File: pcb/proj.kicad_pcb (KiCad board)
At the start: 2 copper layers, 125 x 185 mm, 125 parts, among them J1 Conn_02x05_Odd_Even, SW1 Reset, SW10 8, SW11 9, SW12 /, SW13 Deg/Rad, SW14 Clear, SW15 4, SW16 5, SW17 6, SW18 X, SW19 Constants, SW2 Y/Stats, SW20 Del, SW21 1, SW22 2, SW23 3, SW24 -, SW25 Alpha, SW26 (/), SW27 Sin(x)/Sin-1(x), SW28 Cos(x)/Cos-1(x), SW29 Tan(x)/Tan-1(x), SW3 ./,, SW30 +, SW31 2nd, SW32 Γ(x), SW33 x^y/y√x, SW34 x^2/√x, SW35 log(x)/ln(x), SW36 e^x/10^x, SW37 Graph, SW38 Programs, SW39 Left, SW4 0, SW40 Up, SW41 Right, SW42 Down, SW43 Power, SW44 FPU BOOT0, SW45 Reset, SW5 +/-, SW6 Solve/=, SW7 Sci/Norm, SW8 X/Matrix, SW9 7, U1 PIC16C74, U2 STM32F401RCTx, U3 74HC238, U4 ISL9111EH50Z-T7A, U5 SN74LVC1G32DBVR, Y1 20MHz

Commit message: v 1.2
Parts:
- removed B2: 2032, Parts:BAT_BAT-HLD-001-THM
- B1: value 2032 -> 2x AA; footprint Parts:BAT_BAT-HLD-001-THM -> Battery:BatteryHolder_MPD_BC2AAPC_2xAA
- C1, C2: footprint Capacitor_SMD:C_0402_1005Metric_Pad0.74x0.62mm_HandSolder -> Capacitor_SMD:C_1206_3216Metric_Pad1.33x1.80mm_HandSolder
- D1, D10, D11, D12, D13, D14, D15, D16, D17, D18, D19, D2, D20, D21, D22, D23, D24, D25, D26, D27, D28, D29, D3, D30, D31, D32, D33, D34, D35, D36, D37, D38, D39, D4, D40, D41, D42, D5, D6, D7, D8, D9: value BAS7002 -> S040S2R0; footprint Diode_SMD:D_SOD-523 -> Diode_SMD:D_1206_3216Metric_Pad1.42x1.75mm_HandSolder
- moved B1 11.0 mm to (142.0, 122.0), turned to -90 degrees
- moved J1 4.75 mm to (131.8, 186.8)
- moved D39 0.79 mm to (83.2, 106.2)
- moved D40 0.79 mm to (93.2, 97.8)
- moved D42 0.79 mm to (93.2, 114.8)
- moved D1 0.75 mm to (48.2, 189.0)
- moved D10 0.75 mm to (84.0, 176.8)
- moved D11 0.75 mm to (95.8, 176.8)
- moved D12 0.75 mm to (107.2, 176.8)
- moved D13 0.75 mm to (48.2, 164.5)
- moved D14 0.75 mm to (60.2, 164.5)
- moved D15 0.75 mm to (72.2, 164.5)
- moved D16 0.75 mm to (84.0, 164.5)
- moved D17 0.75 mm to (95.8, 164.5)
- moved D18 0.75 mm to (107.2, 164.5)
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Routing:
- net Net-(B1-+): track 192.7 -> 106.4 mm
- net Net-(D15-K): track 384.4 -> 370.3 mm
- net Net-(D10-K): track 380.2 -> 366.4 mm
- net Net-(D11-K): track 366.7 -> 359.1 mm
- net Net-(D14-K): track 400.8 -> 393.7 mm
- net Net-(D1-K): track 413.9 -> 407.1 mm
- net Net-(D12-K): track 343.6 -> 338.1 mm
- net Net-(D38-A): track 10.2 -> 15.5 mm
- net Net-(D42-A): track 10.2 -> 15.3 mm
- net Net-(D40-A): track 10.2 -> 15.3 mm
- net Net-(D41-A): track 10.0 -> 14.9 mm
- net FPURST: track 111.6 -> 116.4 mm
- net SWO: track 134.1 -> 138.8 mm
- net SWDIO: track 128.2 -> 132.9 mm
- net SWCLK: track 127.1 -> 131.5 mm
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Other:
- board text added: "PICalculator v1.2 Designed by: Kyle Schmerge Max Pastushkov https://github.com/kpzip/PICalculator"
- board text removed: "PICalculator v1.1 Designed by: Kyle Schmerge Max Pastushkov Janet Shen https://github.com/kpzip/PICalculator"

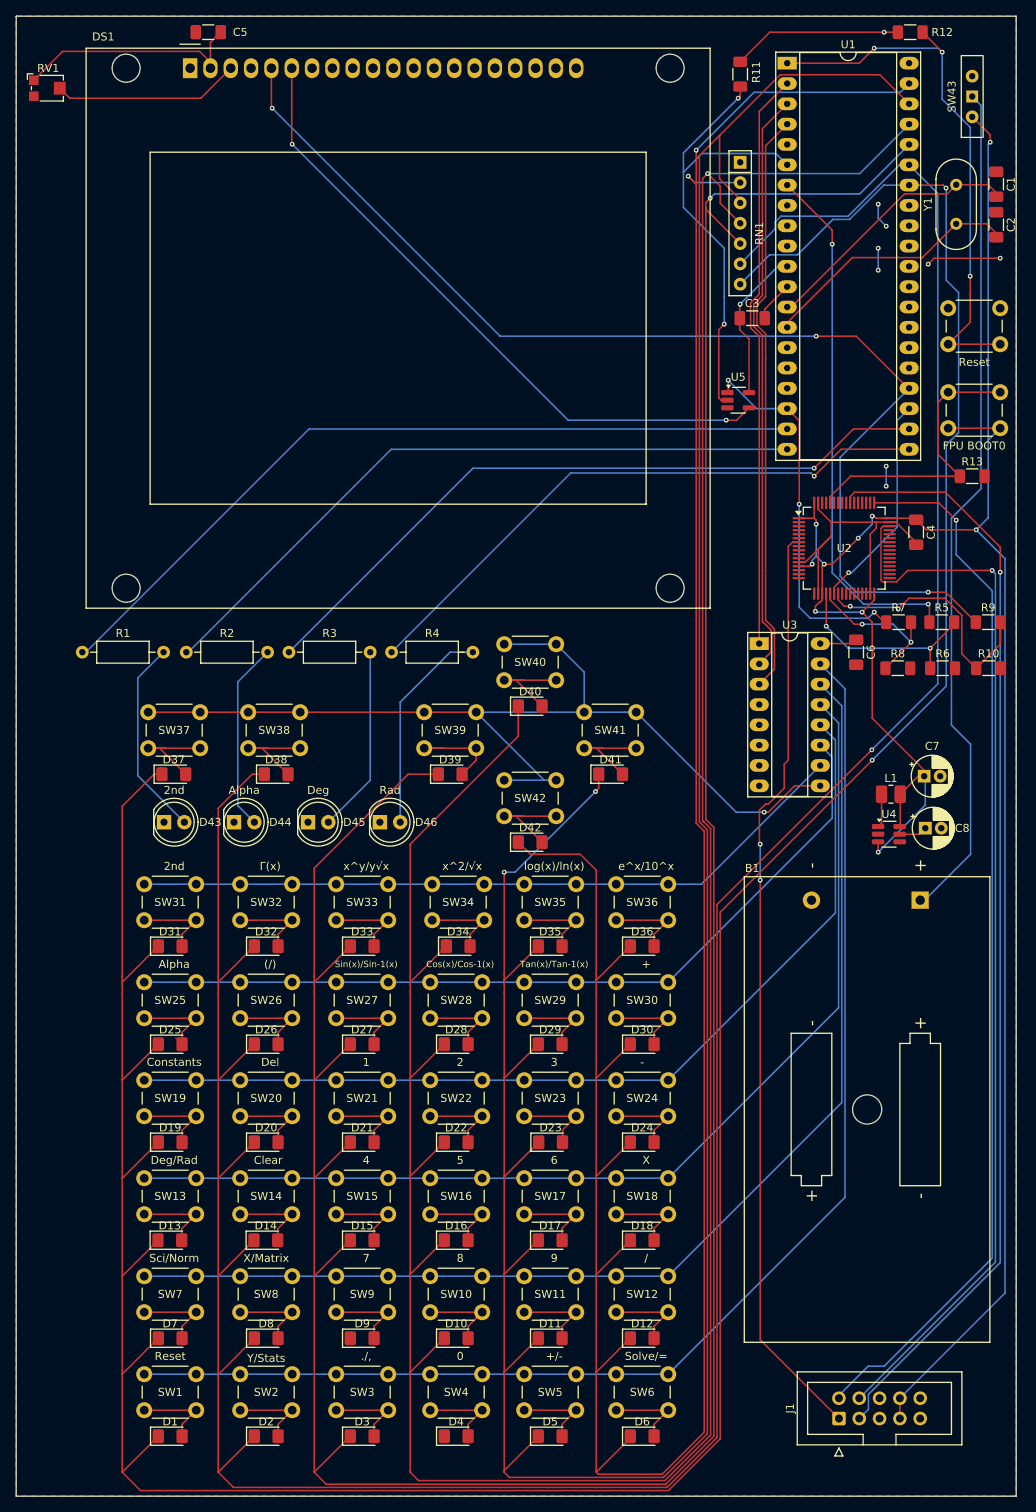
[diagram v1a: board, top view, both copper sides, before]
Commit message: update schematics + add CO RDY trace
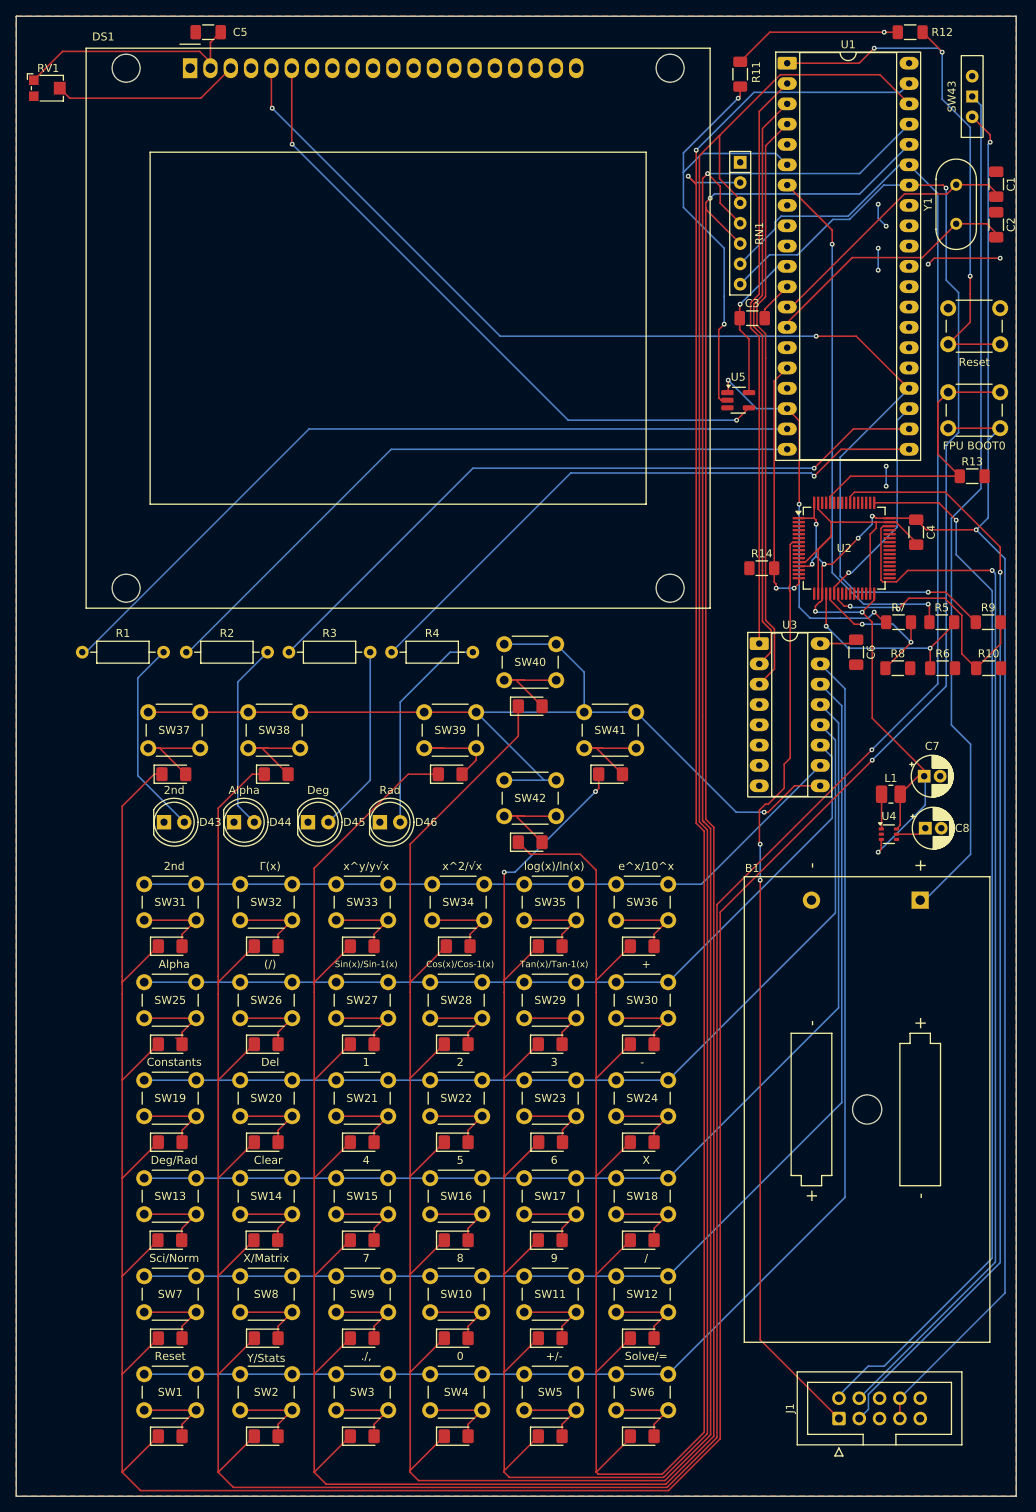
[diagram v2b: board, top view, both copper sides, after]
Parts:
- added R14: 10kΩ, Resistor_SMD:R_1206_3216Metric_Pad1.30x1.75mm_HandSolder, F.Cu at (122.2, 80.5)
- U4: footprint Package_TO_SOT_SMD:SOT-23-6_Handsoldering -> Package_TO_SOT_SMD:SOT-363_SC-70-6
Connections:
- U1 pad 16: unconnected-(U1-CCP2/T1OSI/RC1-Pad16) -> CORDY
- U2 pad 16: unconnected-(U2-PA2-Pad16) -> CORDY
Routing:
- net CORDY: track 0.00 -> 32.0 mm, vias 0 -> 2
- net Net-(D15-K): track 370.3 -> 376.7 mm
- net Net-(D10-K): track 366.4 -> 372.4 mm
- net Net-(D37-A): track 14.7 -> 12.5 mm

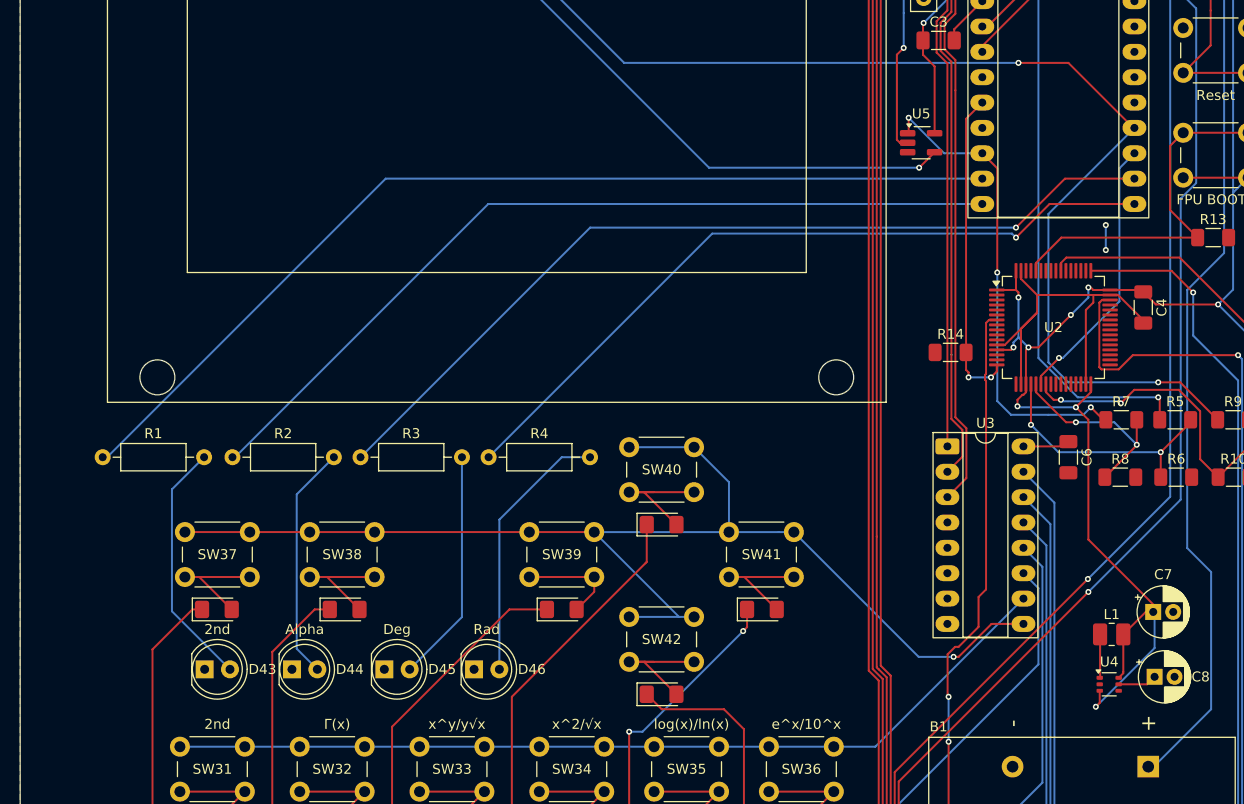
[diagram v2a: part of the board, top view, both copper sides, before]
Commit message: add buzzer and join resets
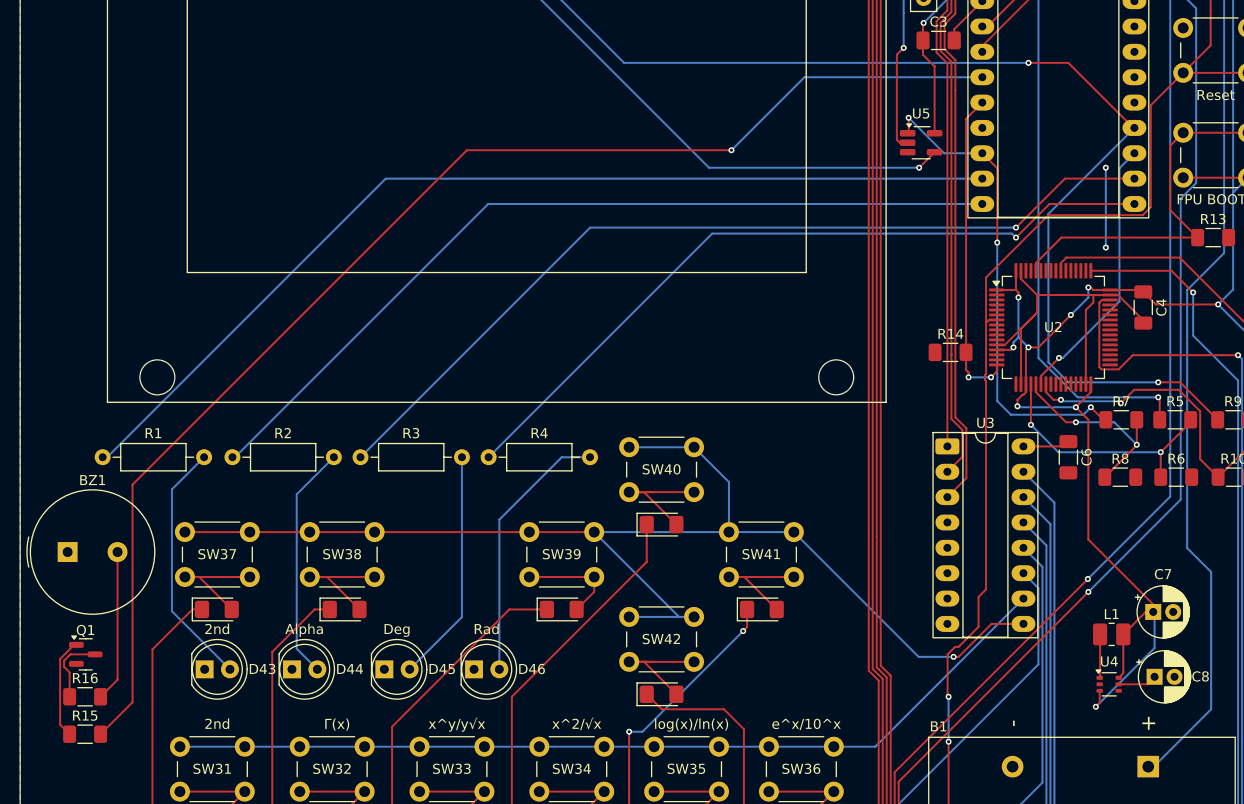
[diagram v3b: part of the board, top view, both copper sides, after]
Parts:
- added BZ1: WT-1205, Buzzer_Beeper:Buzzer_TDK_PS1240P02BT_D12.2mm_H6.5mm, F.Cu at (33.8, 100.5)
- added Q1: MMBT3904, Package_TO_SOT_SMD:SOT-23, F.Cu at (35.6, 110.8)
- added R15: 200Ω, Resistor_SMD:R_1206_3216Metric_Pad1.30x1.75mm_HandSolder, F.Cu at (35.5, 118.8)
- added R16: 200Ω, Resistor_SMD:R_1206_3216Metric_Pad1.30x1.75mm_HandSolder, F.Cu at (35.5, 115.0)
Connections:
- R12 pad 2: Net-(U1-~{MCLR}/Vpp) -> FPURST
- SW45 pad 2: Net-(U1-~{MCLR}/Vpp) -> FPURST
- U1 pad 1: Net-(U1-~{MCLR}/Vpp) -> FPURST
- U1 pad 15: unconnected-(U1-T10S0/T1CKI/RC0-Pad15) -> BUZZ
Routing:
- net BUZZ: track 0.00 -> 128.4 mm, vias 0 -> 1
- net FPURST: track 116.4 -> 225.1 mm, vias 2 -> 5
- net Net-(U1-~{MCLR}/Vpp): track 69.9 -> 0.00 mm, vias 3 -> 0
- net Net-(BZ1--): track 0.00 -> 15.2 mm
- net Net-(Q1-B): track 0.00 -> 10.1 mm
- net Net-(Q1-C): track 0.00 -> 7.21 mm
- net GND: track 52.8 -> 58.3 mm

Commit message: fix
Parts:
- removed R16: 200Ω, Resistor_SMD:R_1206_3216Metric_Pad1.30x1.75mm_HandSolder
- BZ1: footprint Buzzer_Beeper:Buzzer_TDK_PS1240P02BT_D12.2mm_H6.5mm -> Buzzer_Beeper:Buzzer_12x9.5RM7.6
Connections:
- Q1 pad 3: Net-(Q1-C) -> Net-(BZ1--)
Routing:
- net Net-(Q1-C): track 7.21 -> 0.00 mm
- net Net-(BZ1--): track 15.2 -> 12.3 mm
- net Net-(Q1-B): track 10.1 -> 11.2 mm
- net Net-(U2-BOOT0): track 36.7 -> 36.3 mm, vias 0 -> 2

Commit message: fix
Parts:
- U4: footprint Package_TO_SOT_SMD:SOT-363_SC-70-6 -> Package_TO_SOT_SMD:SOT-23-6_Handsoldering
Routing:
- net +3.3V: track 278.3 -> 277.5 mm
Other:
- board text added: "PICalculator v1.3 Designed by: Kyle Schmerge Max Pastushkov https://github.com/kpzip/PICalculator"
- board text removed: "PICalculator v1.2 Designed by: Kyle Schmerge Max Pastushkov https://github.com/kpzip/PICalculator"
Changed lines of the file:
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@@
 		)
 	)
-	(footprint "Package_TO_SOT_SMD:SOT-363_SC-70-6"
+	(footprint "Package_TO_SOT_SMD:SOT-23-6_Handsoldering"
 		(layer "F.Cu")
 		(at 138.0875 113.75)
-		(descr "SOT-363, SC-70-6, SC-88")
-		(tags "SOT-363 SC-70-6 SC-88")
+		(descr "6-pin SOT-23 package, Handsoldering")
+		(tags "SOT-23-6 Handsoldering")
 		(property "Reference" "U4"
-			(at 0 -2.25 0)
+			(at 0 -2.9 0)
 			(layer "F.SilkS")
 			(effects
@@
 		)
 		(property "Value" "ISL9111EH50Z-T7A"
-			(at 0 2 180)
+			(at 0 2.9 0)
 			(layer "F.Fab")
 			(effects
@@
 		(sheetname "/")
 		(sheetfile "proj.kicad_sch")
-		(clearance 0.1)
+		(clearance 0.15)
 		(attr smd)
 		(fp_line
-			(start -0.71 -1.16)
-			(end 0.7 -1.16)
+			(start -0.9 1.61)
+			(end 0.9 1.61)
 			(stroke
 				(width 0.12)
@@
 		)
 		(fp_line
-			(start -0.7 1.16)
-			(end 0.7 1.16)
+			(start 0.1 -1.61)
+			(end -0.7 -1.61)
+			(stroke
+				(width 0.12)
+				(type solid)
+			)
+			(layer "F.SilkS")
+		)
+		(fp_line
+			(start 0.1 -1.61)
+			(end 0.9 -1.61)
 			(stroke
 				(width 0.12)
@@
 		(fp_poly
 			(pts
-				(xy -1.08 -1.11) (xy -1.32 -1.44) (xy -0.84 -1.44) (xy -1.08 -1.11)
+				(xy -1.2 -1.56) (xy -1.44 -1.89) (xy -0.96 -1.89) (xy -1.2 -1.56)
 			)
 			(stroke
@@
 		)
 		(fp_line
-			(start -1.6 -1.4)
-			(end -1.6 1.4)
+			(start -2.4 -1.8)
+			(end 2.4 -1.8)
 			(stroke
 				(width 0.05)
@@
 		)
 		(fp_line
-			(start -1.6 -1.4)
-			(end 1.6 -1.4)
+			(start -2.4 1.8)
+			(end -2.4 -1.8)
 			(stroke
 				(width 0.05)
@@
 		)
 		(fp_line
-			(start -1.6 1.4)
-			(end 1.6 1.4)
+			(start 2.4 -1.8)
+			(end 2.4 1.8)
 			(stroke
 				(width 0.05)
@@
 		)
 		(fp_line
-			(start 1.6 1.4)
-			(end 1.6 -1.4)
+			(start 2.4 1.8)
+			(end -2.4 1.8)
 			(stroke
 				(width 0.05)
@@
 		)
 		(fp_line
-			(start -0.675 -0.6)
-			(end -0.675 1.1)
+			(start -0.9 -0.9)
+			(end -0.9 1.55)
 			(stroke
 				(width 0.1)
@@
 		)
 		(fp_line
-			(start -0.175 -1.1)
-			(end -0.675 -0.6)
+			(start -0.9 -0.9)
+			(end -0.25 -1.55)
 			(stroke
 				(width 0.1)
@@
 		)
 		(fp_line
-			(start 0.675 -1.1)
-			(end -0.175 -1.1)
+			(start 0.9 -1.55)
+			(end -0.25 -1.55)
 			(stroke
 				(width 0.1)
@@
 		)
 		(fp_line
-			(start 0.675 -1.1)
-			(end 0.675 1.1)
+			(start 0.9 -1.55)
+			(end 0.9 1.55)
 			(stroke
 				(width 0.1)
@@
 		)
 		(fp_line
-			(start 0.675 1.1)
-			(end -0.675 1.1)
+			(start 0.9 1.55)
+			(end -0.9 1.55)
 			(stroke
 				(width 0.1)
@@
 		)
 		(pad "1" smd roundrect
-			(at -0.95 -0.65)
-			(size 0.65 0.4)
+			(at -1.35 -0.95)
+			(size 1.56 0.65)
 			(layers "F.Cu" "F.Mask" "F.Paste")
 			(roundrect_rratio 0.25)
@@
 		)
 		(pad "2" smd roundrect
-			(at -0.95 0)
-			(size 0.65 0.4)
+			(at -1.35 0)
+			(size 1.56 0.65)
 			(layers "F.Cu" "F.Mask" "F.Paste")
 			(roundrect_rratio 0.25)
@@
 		)
 		(pad "3" smd roundrect
-			(at -0.95 0.65)
-			(size 0.65 0.4)
+			(at -1.35 0.95)
+			(size 1.56 0.65)
 			(layers "F.Cu" "F.Mask" "F.Paste")
 			(roundrect_rratio 0.25)
@@
 		)
 		(pad "4" smd roundrect
-			(at 0.95 0.65)
-			(size 0.65 0.4)
+			(at 1.35 0.95)
+			(size 1.56 0.65)
 			(layers "F.Cu" "F.Mask" "F.Paste")
 			(roundrect_rratio 0.25)
@@
 		)
 		(pad "5" smd roundrect
-			(at 0.95 0)
-			(size 0.65 0.4)
+			(at 1.35 0)
+			(size 1.56 0.65)
 			(layers "F.Cu" "F.Mask" "F.Paste")
 			(roundrect_rratio 0.25)
@@
 		)
 		(pad "6" smd roundrect
-			(at 0.95 -0.65)
-			(size 0.65 0.4)
+			(at 1.35 -0.95)
+			(size 1.56 0.65)
 			(layers "F.Cu" "F.Mask" "F.Paste")
 			(roundrect_rratio 0.25)
@@
 		)
 		(embedded_fonts no)
-		(model "${KICAD9_3DMODEL_DIR}/Package_TO_SOT_SMD.3dshapes/SOT-363_SC-70-6.wrl"
+		(model "${KICAD9_3DMODEL_DIR}/Package_TO_SOT_SMD.3dshapes/SOT-23-6.wrl"
 			(offset
 				(xyz 0 0 0)
@@
 		(layer "Edge.Cuts")
 	)
-	(gr_text "PICalculator v1.2\nDesigned by:\nKyle Schmerge\nMax Pastushkov\nhttps://github.com/kpzip/PICalculator\n"
+	(gr_text "PICalculator v1.3\nDesigned by:\nKyle Schmerge\nMax Pastushkov\nhttps://github.com/kpzip/PICalculator\n"
 		(at 115.5 46 0)
 		(layer "B.SilkS")
@@
 	)
 	(segment
+		(start 136.75 116)
+		(end 136.75 114.7125)
+		(width 0.2)
+		(layer "F.Cu")
+		(net 4)
+	)
+	(segment
 		(start 142.7625 75.7)
 		(end 141.5 74.4375)
@@
 	)
 	(segment
-		(start 137.1375 114.4)
-		(end 137.1375 115.6125)
-		(width 0.2)
-		(layer "F.Cu")
-		(net 4)
-	)
-	(segment
 		(start 136.7375 115.9875)
 		(end 136.75 116)
@@
 	)
 	(segment
+		(start 136.75 114.7125)
+		(end 136.7375 114.7)
+		(width 0.2)
+		(layer "F.Cu")
+		(net 4)
+	)
+	(segment
 		(start 129 74.5)
 		(end 128.75 74.25)
@@
 	)
 	(segment
+		(start 139.5 108.75)
+		(end 139.5 112.7375)
+		(width 0.2)
+		(layer "F.Cu")
+		(net 4)
+	)
+	(segment
 		(start 128.9 85.9)
 		(end 128.9 85.251471)
@@
 	)
 	(segment
-		(start 139.5 108.75)
-		(end 139.5 112.5)
-		(width 0.2)
-		(layer "F.Cu")
-		(net 4)
-	)
-	(segment
 		(start 129.5 84.75)
 		(end 129.75 84.5)
@@
 	)
 	(segment
-		(start 139.5 112.6375)
-		(end 139.0375 113.1)
-		(width 0.2)
-		(layer "F.Cu")
-		(net 4)
-	)
-	(segment
-		(start 137.1375 115.6125)
-		(end 136.75 116)
-		(width 0.2)
-		(layer "F.Cu")
-		(net 4)
-	)
-	(segment
 		(start 129.401471 84.75)
 		(end 129.5 84.75)
@@
 	)
 	(segment
+		(start 139.5 112.7375)
+		(end 139.4375 112.8)
+		(width 0.2)
+		(layer "F.Cu")
+		(net 4)
+	)
+	(segment
 		(start 136 87.25)
 		(end 136 99.25)
@@
 	)
 	(segment
+		(start 141.882388 113.75)
+		(end 139.4375 113.75)
+		(width 0.2)
+		(layer "F.Cu")
+		(net 145)
+	)
+	(segment
 		(start 34.8 15.9)
 		(end 51.93 15.9)
@@
 	)
 	(segment
-		(start 142.632388 113)
-		(end 141.882388 113.75)
-		(width 0.2)
-		(layer "F.Cu")
-		(net 145)
-	)
-	(segment
 		(start 123.2 13.5)
 		(end 137.5 13.5)
@@
 	)
 	(segment
+		(start 142.632388 113)
+		(end 141.882388 113.75)
+		(width 0.2)
+		(layer "F.Cu")
+		(net 145)
+	)
+	(segment
 		(start 53.28 14.7825)
 		(end 54.5625 13.5)
@@
 		(net 145)
 	)
-	(segment
-		(start 141.882388 113.75)
-		(end 139.0375 113.75)
-		(width 0.2)
-		(layer "F.Cu")
-		(net 145)
-	)
 	(via
 		(at 137.5 13.5)
@@
 	)
 	(segment
-		(start 137.175 108.75)
-		(end 137.175 113.0625)
+		(start 137.175 112.3625)
+		(end 136.7375 112.8)
 		(width 0.2)
 		(layer "F.Cu")
@@
 	)
 	(segment
-		(start 137.175 113.0625)
-		(end 137.1375 113.1)
+		(start 137.175 108.75)
+		(end 137.175 112.3625)
 		(width 0.2)
 		(layer "F.Cu")
